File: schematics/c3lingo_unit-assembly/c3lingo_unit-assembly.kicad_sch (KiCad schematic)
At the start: 0 parts

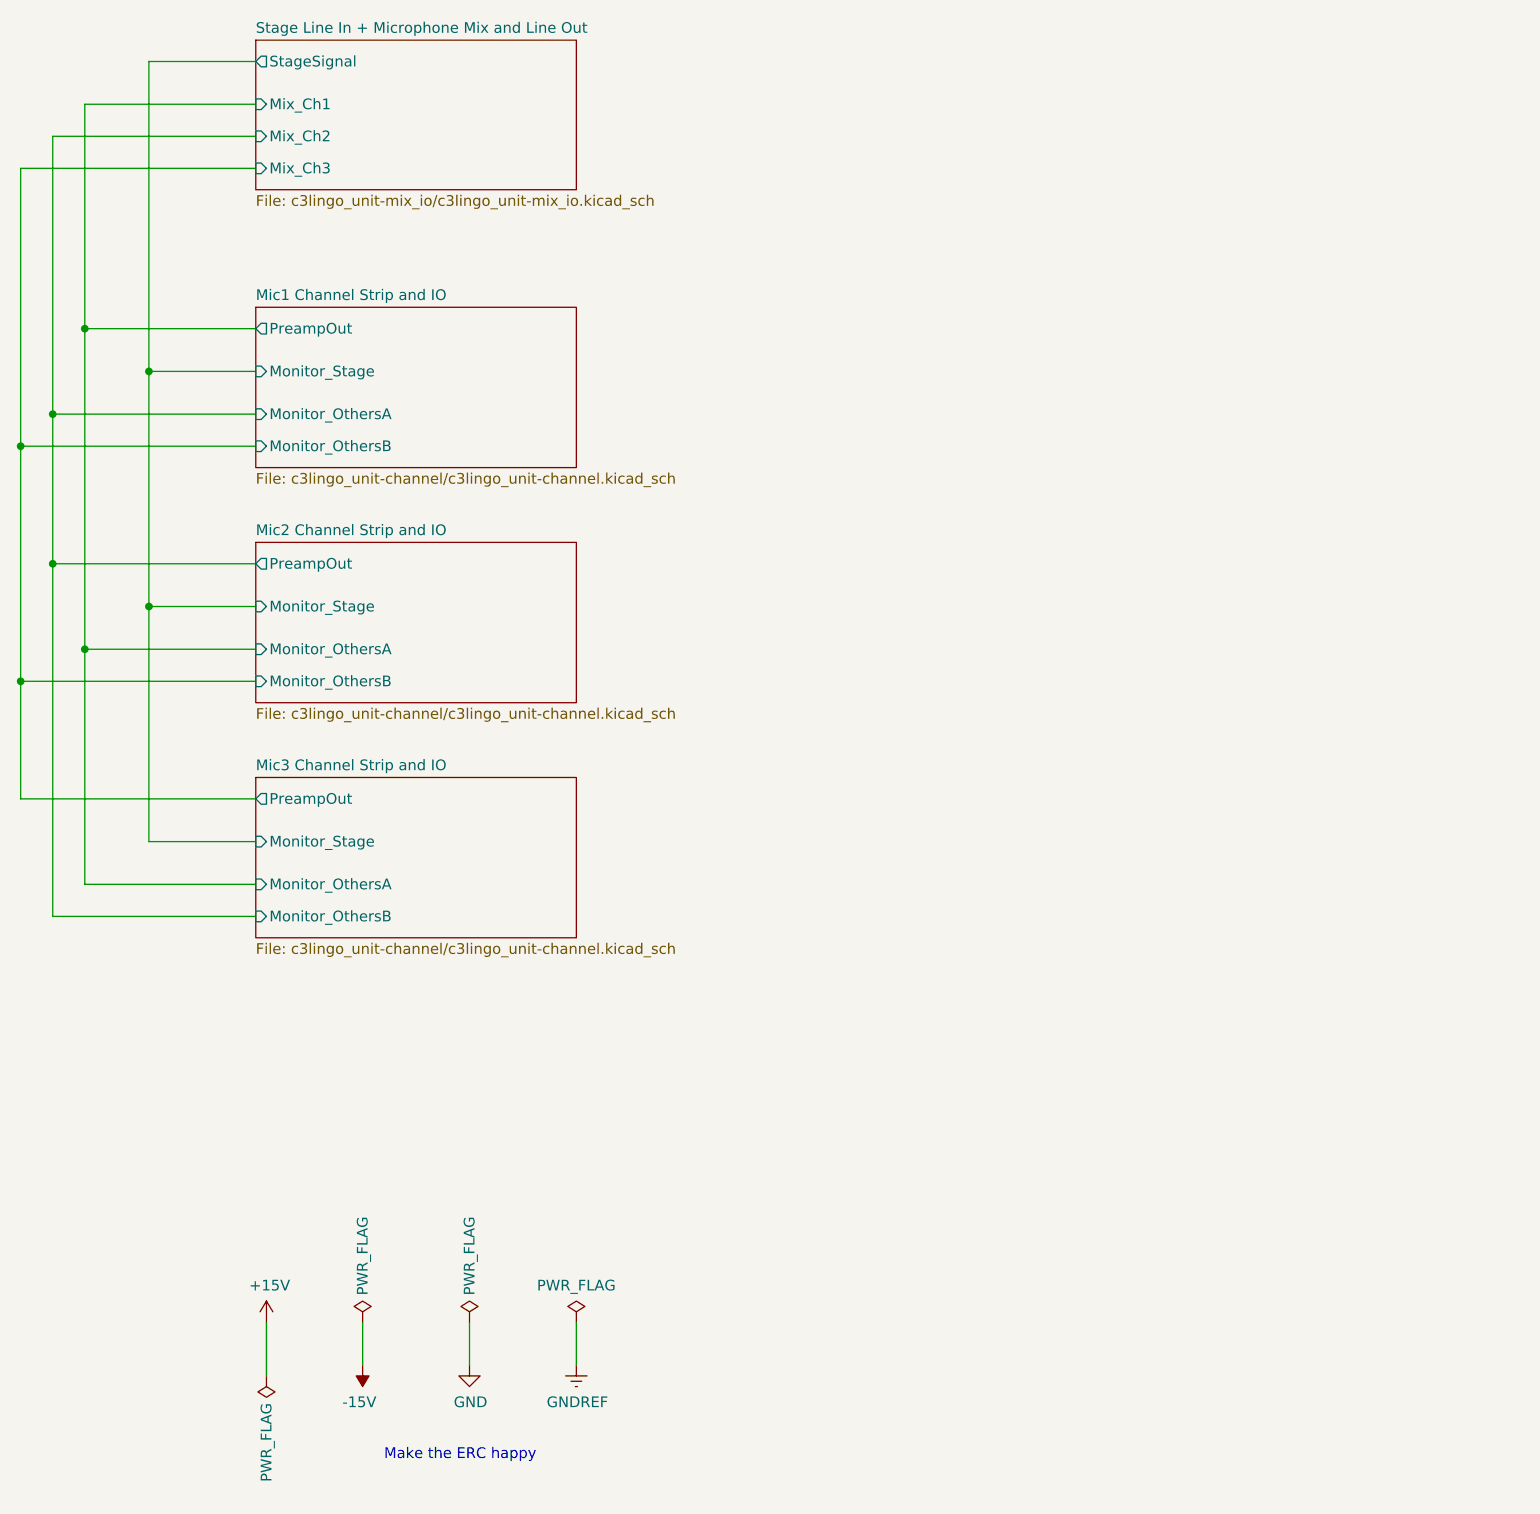
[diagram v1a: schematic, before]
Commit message: [TIDY] Split channel into two schematics
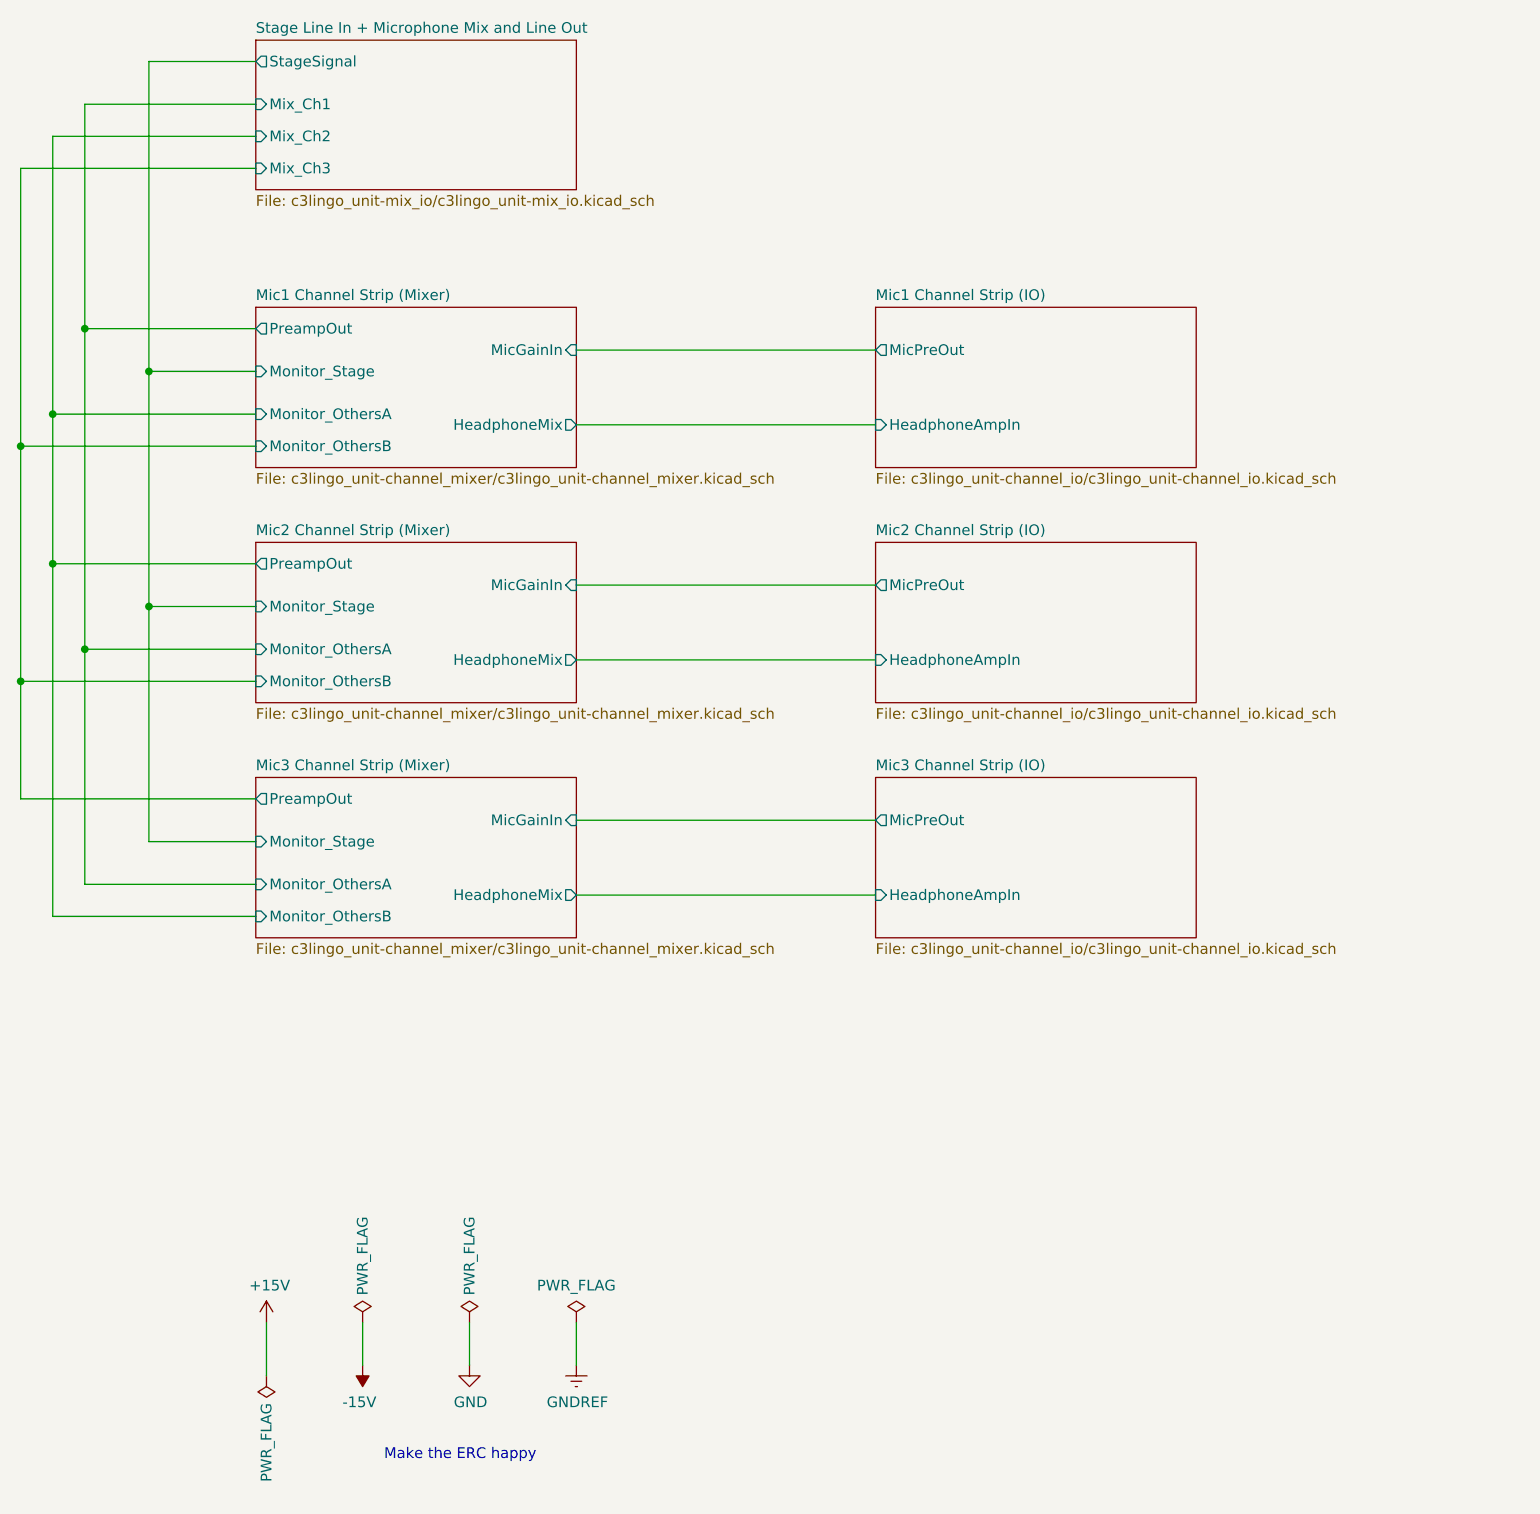
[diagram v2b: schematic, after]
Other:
- sheet Mic1 Channel Strip and IO renamed Mic1 Channel Strip (Mixer)
- sheet Mic2 Channel Strip and IO renamed Mic2 Channel Strip (Mixer)
- sheet Mic3 Channel Strip and IO renamed Mic3 Channel Strip (Mixer)
- added sheet Mic1 Channel Strip (IO) (c3lingo_unit-channel_io/c3lingo_unit-channel_io.kicad_sch)
- added sheet Mic2 Channel Strip (IO) (c3lingo_unit-channel_io/c3lingo_unit-channel_io.kicad_sch)
- added sheet Mic3 Channel Strip (IO) (c3lingo_unit-channel_io/c3lingo_unit-channel_io.kicad_sch)
- sheet Mic1 Channel Strip (Mixer): file c3lingo_unit-channel/c3lingo_unit-channel.kicad_sch -> c3lingo_unit-channel_mixer/c3lingo_unit-channel_mixer.kicad_sch
- sheet Mic1 Channel Strip (Mixer) ports: added HeadphoneMix, MicGainIn; removed none
- sheet Mic2 Channel Strip (Mixer): file c3lingo_unit-channel/c3lingo_unit-channel.kicad_sch -> c3lingo_unit-channel_mixer/c3lingo_unit-channel_mixer.kicad_sch
- sheet Mic2 Channel Strip (Mixer) ports: added HeadphoneMix, MicGainIn; removed none
- sheet Mic3 Channel Strip (Mixer): file c3lingo_unit-channel/c3lingo_unit-channel.kicad_sch -> c3lingo_unit-channel_mixer/c3lingo_unit-channel_mixer.kicad_sch
- sheet Mic3 Channel Strip (Mixer) ports: added HeadphoneMix, MicGainIn; removed none

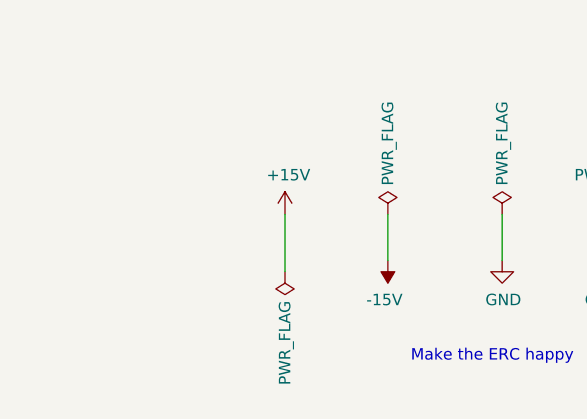
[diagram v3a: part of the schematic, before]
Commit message: new headphone amp IC (board layout not updated)
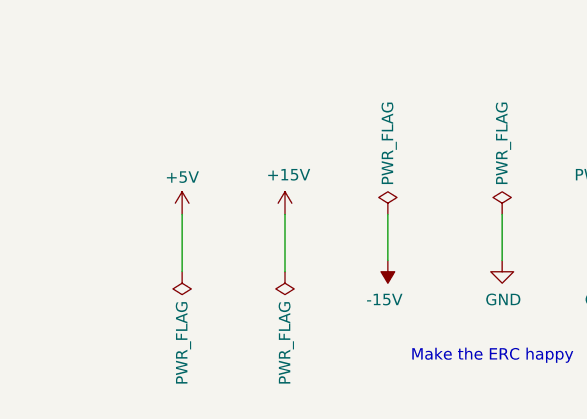
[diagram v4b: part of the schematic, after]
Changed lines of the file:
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@@
   (title_block
     (title "c3lingo interpeter unit")
-    (date "2023-01-04")
+    (date "2024-03-04")
     (rev "v0.3.0")
     (company "Jannik Beyerstedt (jtbx)")
@@
     (stroke (width 0) (type default))
   )
+  (wire (pts (xy 116.84 177.8) (xy 116.84 184.15))
+    (stroke (width 0) (type default))
+  )
   (wire (pts (xy 127 27.94) (xy 114.3 27.94))
     (stroke (width 0) (type default))
@@
     )
   )
+  (symbol (lib_id "power:+5V") (at 116.84 177.8 0) (unit 1)
+    (in_bom yes) (on_board yes) (dnp no) (fields_autoplaced)
+    (property "Reference" "#PWR0105" (at 116.84 181.61 0)
+      (effects (font (size 1.27 1.27)) hide)
+    )
+    (property "Value" "+5V" (at 116.84 173.6669 0)
+      (effects (font (size 1.27 1.27)))
+    )
+    (property "Footprint" "" (at 116.84 177.8 0)
+      (effects (font (size 1.27 1.27)) hide)
+    )
+    (property "Datasheet" "" (at 116.84 177.8 0)
+      (effects (font (size 1.27 1.27)) hide)
+    )
+    (pin "1")
+    (instances
+      (project "c3lingo_unit-assembly"
+        (path "/9e80d1ee-62c1-483d-830d-f559e7294d20"
+          (reference "#PWR0105") (unit 1)
+        )
+      )
+    )
+  )
   (symbol (lib_id "power:PWR_FLAG") (at 139.7 177.8 0) (unit 1)
     (in_bom yes) (on_board yes) (dnp no)
@@
         )
       )
+    )
+  )
+  (symbol (lib_id "power:PWR_FLAG") (at 116.84 184.15 180) (unit 1)
+    (in_bom yes) (on_board yes) (dnp no)
+    (property "Reference" "#FLG0105" (at 116.84 186.055 0)
+      (effects (font (size 1.27 1.27)) hide)
+    )
+    (property "Value" "PWR_FLAG" (at 116.84 187.3758 90)
+      (effects (font (size 1.27 1.27)) (justify left))
+    )
+    (property "Footprint" "" (at 116.84 184.15 0)
+      (effects (font (size 1.27 1.27)) hide)
+    )
+    (property "Datasheet" "~" (at 116.84 184.15 0)
+      (effects (font (size 1.27 1.27)) hide)
+    )
+    (pin "1")
+    (instances
+      (project "c3lingo_unit-assembly"
+        (path "/9e80d1ee-62c1-483d-830d-f559e7294d20"
+          (reference "#FLG0105") (unit 1)
+        )
+      )
